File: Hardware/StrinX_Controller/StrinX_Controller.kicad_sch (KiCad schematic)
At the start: 0 parts

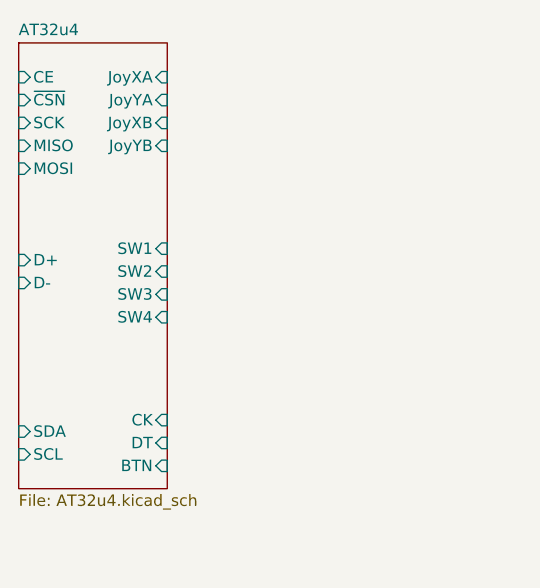
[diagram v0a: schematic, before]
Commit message: Add USB-C schematic module
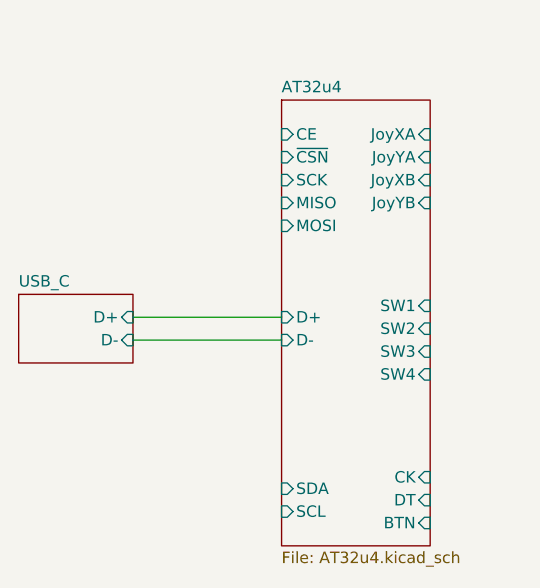
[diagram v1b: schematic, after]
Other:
- added sheet USB_C (USB_C.kicad_sch)
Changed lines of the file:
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@@
 	(generator_version "9.0")
 	(paper "A4")
+	(wire
+		(pts
+			(xy 127 93.98) (xy 143.51 93.98)
+		)
+		(stroke
+			(width 0)
+			(type default)
+		)
+	)
+	(wire
+		(pts
+			(xy 127 96.52) (xy 143.51 96.52)
+		)
+		(stroke
+			(width 0)
+			(type default)
+		)
+	)
 	(sheet
-		(at 114.3 63.5)
+		(at 114.3 91.44)
+		(size 12.7 7.62)
+		(exclude_from_sim no)
+		(in_bom yes)
+		(on_board yes)
+		(dnp no)
+		(fields_autoplaced yes)
+		(stroke
+			(width 0.1524)
+			(type solid)
+		)
+		(fill
+			(color 0 0 0 0.0000)
+		)
+		(property "Sheetname" "USB_C"
+			(at 114.3 90.7284 0)
+			(effects
+				(font
+					(size 1.27 1.27)
+				)
+				(justify left bottom)
+			)
+		)
+		(property "Sheetfile" "USB_C.kicad_sch"
+			(at 114.3 99.6446 0)
+			(effects
+				(font
+					(size 1.27 1.27)
+				)
+				(justify left top)
+				(hide yes)
+			)
+		)
+		(pin "D-" input
+			(at 127 96.52 0)
+			(effects
+				(font
+					(size 1.27 1.27)
+				)
+				(justify right)
+			)
+		)
+		(pin "D+" input
+			(at 127 93.98 0)
+			(effects
+				(font
+					(size 1.27 1.27)
+				)
+				(justify right)
+			)
+		)
+		(instances
+			(project "StrinX_Controller"
+				(path "/60efaa1b-44bb-4814-90d0-8b9990f45080"
+					(page "3")
+				)
+			)
+		)
+	)
+	(sheet
+		(at 143.51 69.85)
 		(size 16.51 49.53)
 		(exclude_from_sim no)
@@
 		)
 		(property "Sheetname" "AT32u4"
-			(at 114.3 62.7884 0)
+			(at 143.51 69.1384 0)
 			(effects
 				(font
@@
 		)
 		(property "Sheetfile" "AT32u4.kicad_sch"
-			(at 114.3 113.6146 0)
+			(at 143.51 119.9646 0)
 			(effects
 				(font
@@
 		)
 		(pin "SCL" input
-			(at 114.3 109.22 180)
+			(at 143.51 115.57 180)
 			(effects
 				(font
@@
 		)
 		(pin "JoyXB" input
-			(at 130.81 72.39 0)
+			(at 160.02 78.74 0)
 			(effects
 				(font
@@
 		)
 		(pin "CK" input
-			(at 130.81 105.41 0)
+			(at 160.02 111.76 0)
 			(effects
 				(font
@@
 		)
 		(pin "SW4" input
-			(at 130.81 93.98 0)
+			(at 160.02 100.33 0)
 			(effects
 				(font
@@
 		)
 		(pin "JoyYA" input
-			(at 130.81 69.85 0)
+			(at 160.02 76.2 0)
 			(effects
 				(font
@@
 		)
 		(pin "SW2" input
-			(at 130.81 88.9 0)
+			(at 160.02 95.25 0)
 			(effects
 				(font
@@
 		)
 		(pin "SW3" input
-			(at 130.81 91.44 0)
+			(at 160.02 97.79 0)
 			(effects
 				(font
@@
 		)
 		(pin "MISO" input
-			(at 114.3 74.93 180)
+			(at 143.51 81.28 180)
 			(effects
 				(font
@@
 		)
 		(pin "JoyXA" input
-			(at 130.81 67.31 0)
+			(at 160.02 73.66 0)
 			(effects
 				(font
@@
 		)
 		(pin "D+" input
-			(at 114.3 87.63 180)
+			(at 143.51 93.98 180)
 			(effects
 				(font
@@
 		)
 		(pin "SDA" input
-			(at 114.3 106.68 180)
+			(at 143.51 113.03 180)
 			(effects
 				(font
@@
 		)
 		(pin "CE" input
-			(at 114.3 67.31 180)
+			(at 143.51 73.66 180)
 			(effects
 				(font
@@
 		)
 		(pin "D-" input
-			(at 114.3 90.17 180)
+			(at 143.51 96.52 180)
 			(effects
 				(font
@@
 		)
 		(pin "JoyYB" input
-			(at 130.81 74.93 0)
+			(at 160.02 81.28 0)
 			(effects
 				(font
@@
 		)
 		(pin "SCK" input
-			(at 114.3 72.39 180)
+			(at 143.51 78.74 180)
 			(effects
 				(font
@@
 		)
 		(pin "DT" input
-			(at 130.81 107.95 0)
+			(at 160.02 114.3 0)
 			(effects
 				(font
@@
 		)
 		(pin "~{CSN}" input
-			(at 114.3 69.85 180)
+			(at 143.51 76.2 180)
 			(effects
 				(font
@@
 		)
 		(pin "MOSI" input
-			(at 114.3 77.47 180)
+			(at 143.51 83.82 180)
 			(effects
 				(font
@@
 		)
 		(pin "BTN" input
-			(at 130.81 110.49 0)
+			(at 160.02 116.84 0)
 			(effects
 				(font
@@
 		)
 		(pin "SW1" input
-			(at 130.81 86.36 0)
-			(effects
-				(font
+			(at 160.02 92.71 0)
+			(effects
+				(font
